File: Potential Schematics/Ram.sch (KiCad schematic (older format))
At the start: 6 parts, among them U25 74LS04, U30 74LS09, U31 74LS09, U32 74LS09, U33 74LS09, U34 74LS09

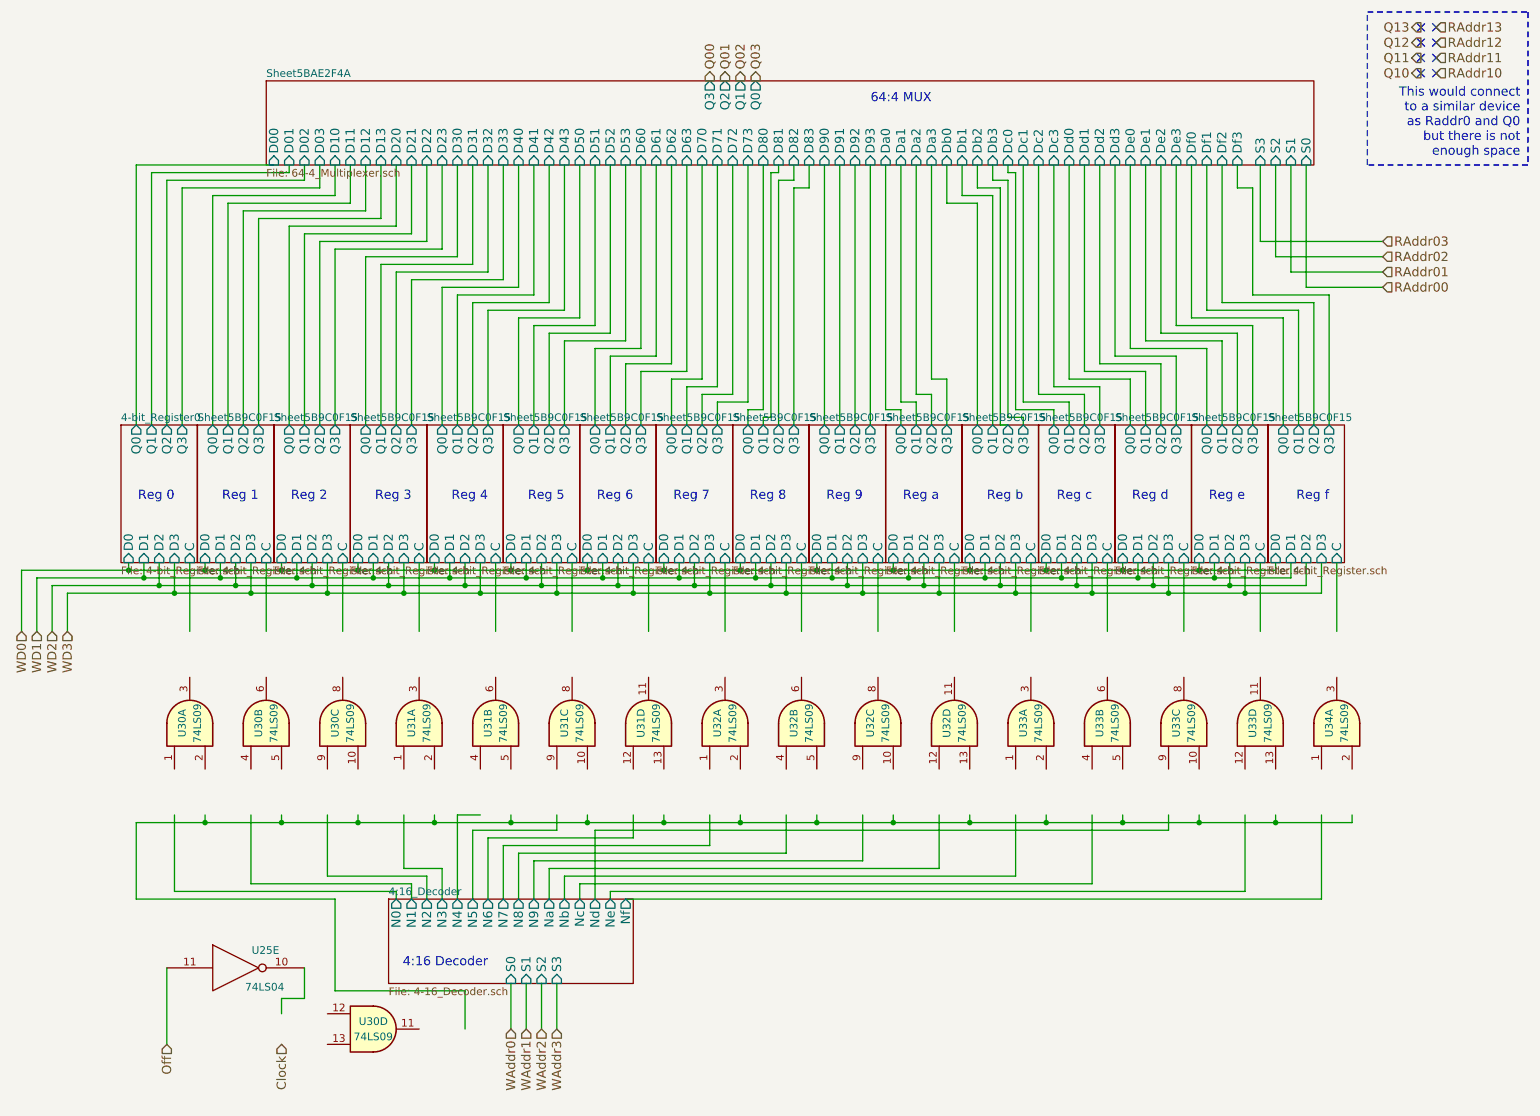
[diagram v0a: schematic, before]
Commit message: Updated overview of Schematic
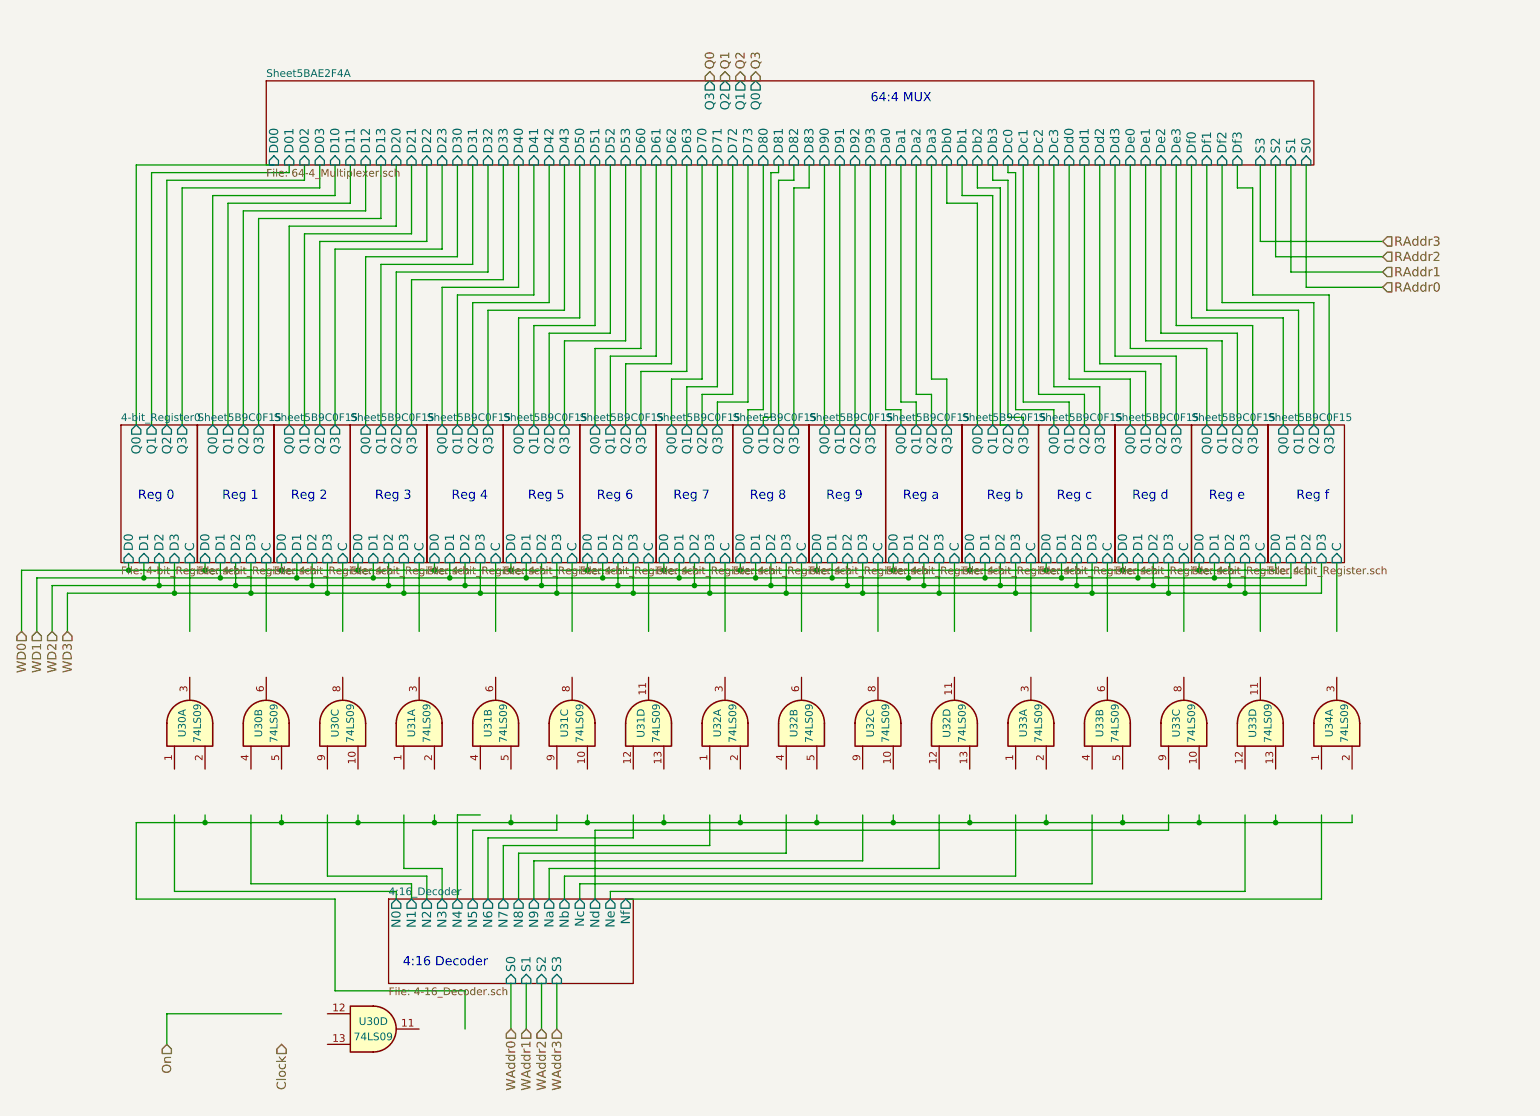
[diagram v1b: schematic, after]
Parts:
- removed U25: 74LS04, Daniel_Kopp:DIP-14_300_ELL, symbol 4-bit_processor-rescue:74LS04
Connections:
- net labels added: On, Q0, Q1, Q2, Q3, RAddr0, RAddr1, RAddr2, RAddr3
- net labels removed: Off, Q00, Q01, Q02, Q03, Q10, Q11, Q12, Q13, RAddr00, RAddr01, RAddr02, RAddr03, RAddr10, RAddr11, RAddr12, RAddr13
- wire segments 439 -> 437
- no-connect marks 8 -> 0
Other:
- note removed: "This would connect\nto a similar device\nas Raddr0 and Q0 \nbut there is not \nenough space\n"
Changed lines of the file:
@@
 $Descr A4 11693 8268
 encoding utf-8
-Sheet 23 902
+Sheet 475 902
 Title "Registers / Cache"
 Date "2018-09-14"
@@
 $EndDescr
 Text HLabel 9950 2450 2    60   Input ~ 0
-RAddr00
+RAddr0
 Text HLabel 9950 2350 2    60   Input ~ 0
-RAddr01
+RAddr1
 Text HLabel 9950 2250 2    60   Input ~ 0
-RAddr02
+RAddr2
 Text HLabel 9950 2150 2    60   Input ~ 0
-RAddr03
-Text HLabel 10300 1050 2    60   Input ~ 0
-RAddr10
-Text HLabel 10300 950  2    60   Input ~ 0
-RAddr11
-Text HLabel 10300 850  2    60   Input ~ 0
-RAddr12
-Text HLabel 10300 750  2    60   Input ~ 0
-RAddr13
+RAddr3
 Text HLabel 2750 7400 3    60   Input ~ 0
 Clock
@@
 WAddr3
 Text HLabel 5550 1100 1    60   Output ~ 0
-Q00
+Q0
 Text HLabel 5650 1100 1    60   Output ~ 0
-Q01
+Q1
 Text HLabel 5750 1100 1    60   Output ~ 0
-Q02
+Q2
 Text HLabel 5850 1100 1    60   Output ~ 0
-Q03
-Text HLabel 10200 1050 0    60   Output ~ 0
-Q10
-Text HLabel 10200 950  0    60   Output ~ 0
-Q11
-Text HLabel 10200 850  0    60   Output ~ 0
-Q12
-Text HLabel 10200 750  0    60   Output ~ 0
-Q13
+Q3
 $Sheet
 S 1700 3350 500  900
@@
 $EndSheet
 Text HLabel 2000 7400 3    60   Input ~ 0
-Off
+On
 $Comp
 L 4-bit_processor-rescue:74LS09 U30
@@
 F 3 "" H 3350 7300 50  0001 C CNN
 	4    3350 7300
-	1    0    0    -1
-$EndComp
-$Comp
-L 4-bit_processor-rescue:74LS04 U25
-U 5 1 5B9CA481
-P 2450 6900
-F 0 "U25" H 2645 7015 50  0000 C CNN
-F 1 "74LS04" H 2640 6775 50  0000 C CNN
-F 2 "Daniel_Kopp:DIP-14_300_ELL" H 2450 6900 50  0001 C CNN
-F 3 "" H 2450 6900 50  0001 C CNN
-	5    2450 6900
 	1    0    0    -1
 $EndComp
@@
 $EndSheet
 Wire Wire Line
-	2000 7400 2000 6900
-Wire Wire Line
-	2900 6900 2900 7100
-Wire Wire Line
-	2900 7100 2750 7100
-Wire Wire Line
-	2750 7100 2750 7200
+	2000 7400 2000 7200
 Wire Wire Line
 	3950 7300 3950 7050
@@
 Connection ~ 9250 5950
 Wire Wire Line
-	4250 7000 4250 7300
-Wire Wire Line
-	4350 7000 4350 7300
-Wire Wire Line
-	4450 7000 4450 7300
-Wire Wire Line
-	4550 7000 4550 7300
-Wire Wire Line
 	2050 5900 2050 6400
 Wire Wire Line
@@
 Wire Wire Line
 	6700 3250 6700 1650
-NoConn ~ 10200 750
-NoConn ~ 10200 850
-NoConn ~ 10200 950
-NoConn ~ 10200 1050
-NoConn ~ 10300 750
-NoConn ~ 10300 850
-NoConn ~ 10300 950
-NoConn ~ 10300 1050
-Text Notes 10850 1600 2    60   ~ 0
-This would connect\nto a similar device\nas Raddr0 and Q0 \nbut there is not \nenough space\n
-Wire Notes Line
-	9850 650  10900 650
-Wire Notes Line
-	10900 650  10900 1650
-Wire Notes Line
-	10900 1650 9850 1650
-Wire Notes Line
-	9850 1650 9850 650
 Text Notes 2050 3850 2    60   ~ 0
 Reg 0\n
@@
 Wire Wire Line
 	9050 4450 9550 4450
+Wire Wire Line
+	4550 7000 4550 7300
+Wire Wire Line
+	4450 7000 4450 7300
+Wire Wire Line
+	4350 7000 4350 7300
+Wire Wire Line
+	4250 7000 4250 7300
+Wire Wire Line
+	2000 7200 2750 7200
 $EndSCHEMATC
